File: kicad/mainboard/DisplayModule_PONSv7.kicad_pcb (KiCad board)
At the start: 4 copper layers, 55.4 x 77.6 mm, 135 parts, among them J1 Ext. Speaker, J2 54132-4062, J3 2005280040, J4 Micro_SD_Card_Det2, J5 Conn_01x03_Shielded, J6 USB_B_Micro, Q1 AO3401A, SW1 PTS645VK392LFS, SW2 SW_TS-1088, SW3 SW_TS-1088, U1 PAM8302AADCR, U10 BNO085, U12 E220-900T22S(JP), U2 W25Q128JVS, U3 RP2350_80QFN, U4 MCP73831-2-OT, U5 TPS63031DSK, U6 MAINSW_CUS-12TB, U7 TFTSW_CUS-12TB, U8 MS5611-01BA, Y1 X322512MSB4SI, Y2 32.768k

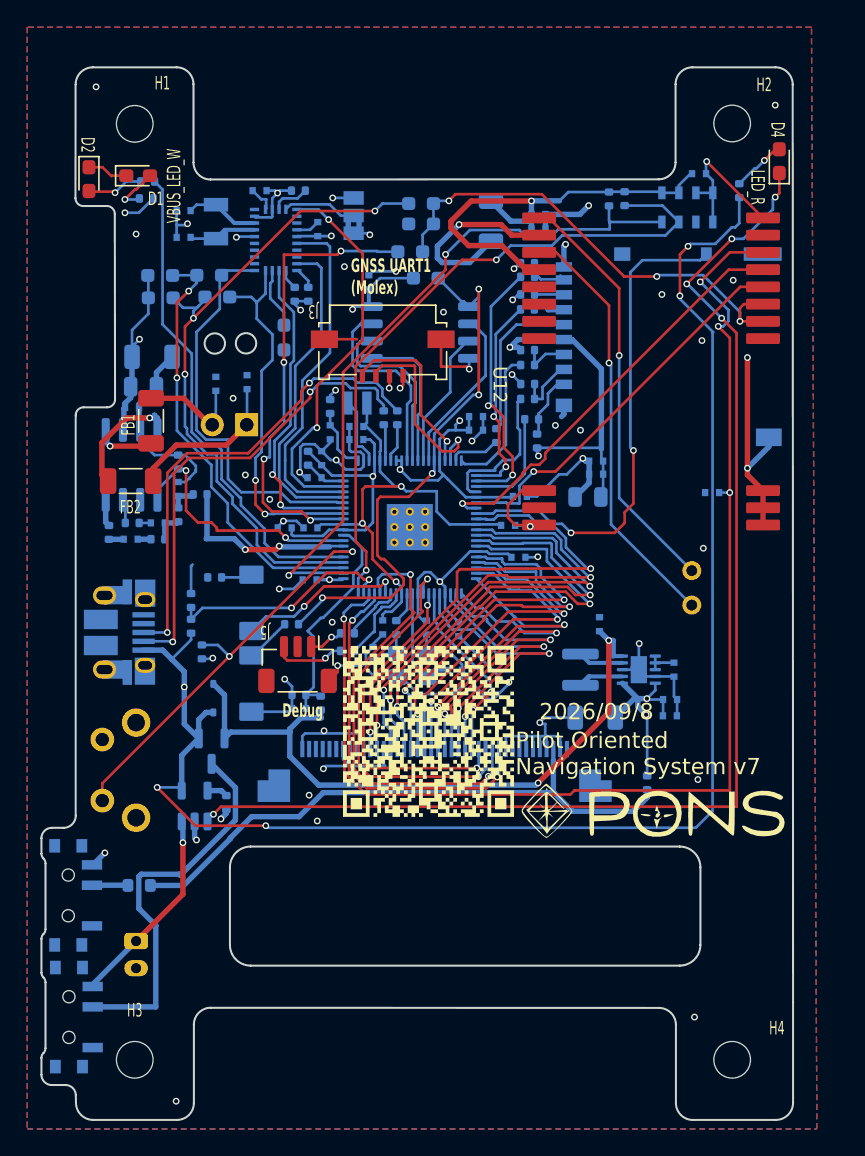
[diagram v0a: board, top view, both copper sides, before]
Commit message: 0.986 新基板（SCH16T 外付け）の kicad を追加し、ガーバー出力を git から外した
kicad/IMU_murata/ — SCH16T-K01-10 のブレイクアウト（新規）
本体の J7（Molex 200528-0080・8pin FPC）へ 1:1 ケーブルで繋ぐ外付け基板。
J1 のピン順を本体 J7 と一致させてある（1=+3V3 2=RESET 3=MOSI 4=CS 5=SCK
6=SYNC 7=MISO 8=GND）。シンボルとフットプリントも同梱。
- ★ R2（CS-GND の 4.7k）は実装しない。CS は負論理なので、プルダウンすると
  MCU が駆動していない間セレクト状態になる。R1（EXTRESN プルアップ）は実装する
- 本体側の GPIO 割り当ては settings.h の SCH16T_PIN_* が正本
  （一覧は docs/imu_sch16t_plan.md §3）

mainboard / GNSS モジュールの更新
- mainboard: DisplayModule_PONSv7 の pcb / pro / sch、MS5611BNO085.kicad_sch、
  SHT_RP2354B.kicad_sch
- GNSS モジュール: pcb / pro / sch、および QRv7 と FPC 4p のフットプリントを
  同プロジェクトの Footprints/ へ取り込み

kicad/FPC/ を畳んだ
FPC コネクタ 1 個のためのプロジェクトだったので、フットプリントを
kicad/GNSSboard_SAM-M10Q/Footprints/ へ移して削除した。
中身は同じで、差分は KiCad が再生成する uuid だけ。

ガーバー・ドリルのプロット出力を git から外した
kicad/.gitignore に追加（*.gbr *.gbl *.gbs *.gbp *.gbo *.gm1 *.gtl *.gts
*.gtp *.gto *.drl と、保険の *plot/ *plot.zip）。発注のたびに作り直せるうえ、
基板を直すたびに巨大な差分になる（ルート .gitignore の production/ と同じ理由）。
★ 入れ物のフォルダ名で書かないこと。v5_1plot/ のような名前は付け方が毎回違うので
  次の基板で外れる。既存の *-backups/ / *.kicad_prl と同じ方針。

Co-Authored-By: Claude Opus 5 <noreply@anthropic.com>
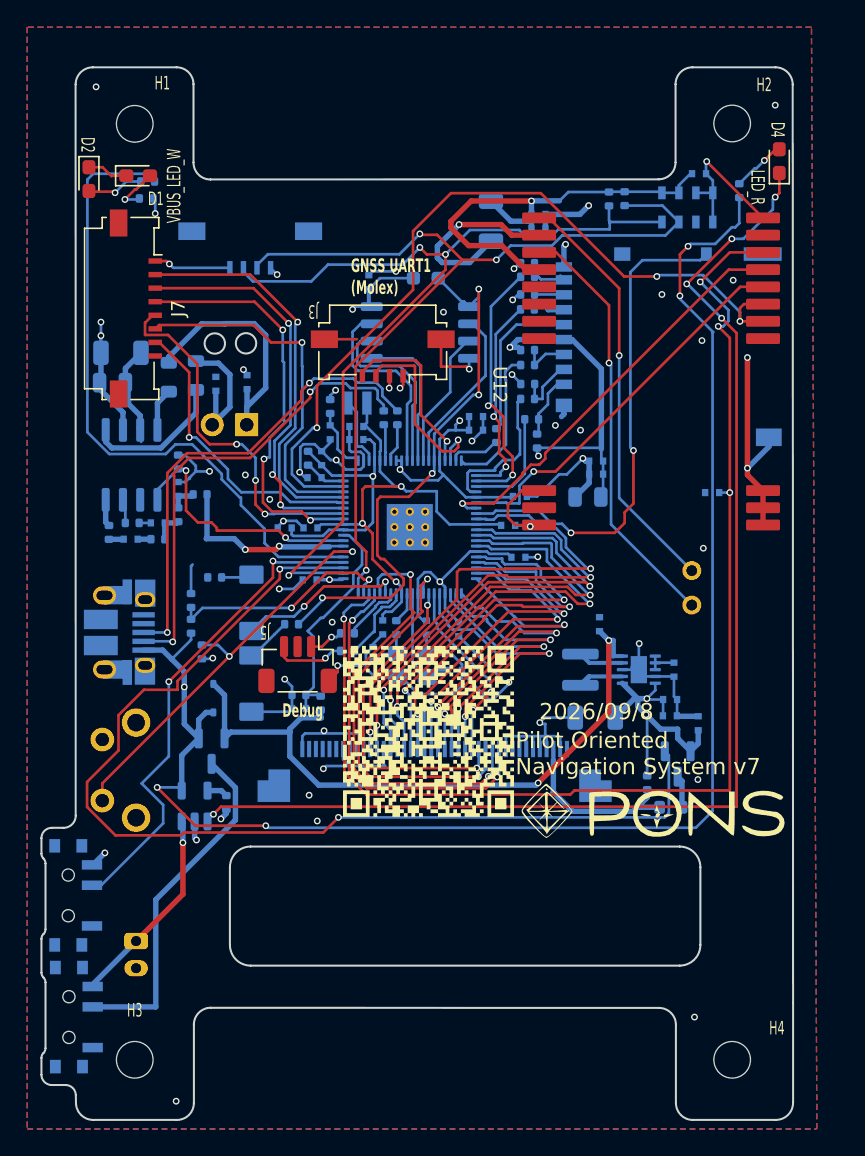
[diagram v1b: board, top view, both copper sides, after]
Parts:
- removed C40: 100n, GPS_TFT:C_0402_1005Metric_small_pads
- removed C41, C42: 15p, GPS_TFT:C_0402_1005Metric_small_pads
- removed JP1: BNO_I2C_SPI_SELECT, Jumper:SolderJumper-3_P1.3mm_Bridged2Bar12_Pad1.0x1.5mm
- removed R37, R38: 4.7k, Resistor_SMD:R_0603_1608Metric_Pad0.98x0.95mm_HandSolder
- removed R44: 10k, Resistor_SMD:R_0402_1005Metric
- removed R46, R47, R50, R51, R52, R53: 0, Resistor_SMD:R_0603_1608Metric_Pad0.98x0.95mm_HandSolder
- removed R48, R49: 4.7k, Resistor_SMD:R_0402_1005Metric
- removed U10: BNO085, GPS_TFT:bno085
- removed Y2: 32.768k, Crystal:Crystal_SMD_3215-2Pin_3.2x1.5mm
- added J7: Conn_01x08_MountingPin, Connector_FFC-FPC:Molex_200528-0080_1x08-1MP_P1.00mm_Horizontal, F.Cu at (102.6, 72.5)
- added J8: 2005280040, Connector_FFC-FPC:Molex_200528-0040_1x04-1MP_P1.00mm_Horizontal, B.Cu at (110.5, 68.6)
- added Q2: AO3401A, Package_TO_SOT_SMD:SOT-23, B.Cu at (142.0, 106.1)
- C39: value 100n -> 10u
- FB1, FB2: value 390 -> 600; footprint Inductor_SMD:L_1206_3216Metric_Pad1.22x1.90mm_HandSolder -> Inductor_SMD:L_0805_2012Metric; moved to B.Cu
- moved C39 50.8 mm to (143.5, 103.1), turned to 90 degrees
- moved R9 39.6 mm to (141.5, 109.3), turned to 180 degrees
- moved FB2 8.15 mm to (104.5, 77.6), turned to 90 degrees
- moved FB1 4.70 mm to (106.5, 77.4)
- moved C7 2.31 mm to (100.3, 78.0)
- moved C9 2.31 mm to (101.0, 75.8)
- moved C6 0.86 mm to (101.0, 79.5)
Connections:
- R9 pad 1: PWR_TFT -> Net-(Q2-D)
- U12 pad 5: Net-(U12-M0) -> LORA_M01
- U12 pad 6: Net-(U12-M0) -> LORA_M01
- U3 pad 43: I2C1_SDA -> TFT_MOSFET_G
- U3 pad 44: I2C1_SCL -> TFT_SW
- U3 pad 56: BNO_INT -> SCH16T_RESET
- U3 pad 57: BNO_NRST -> SCH16T_SYNC
- U3 pad 58: BNO_WAKE -> LORA_M01
- U7 pad P$2: PWR_TFT -> TFT_SW
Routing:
- net TFT_MOSFET_G: track 0.00 -> 78.7 mm, vias 0 -> 2
- net LORA_M01: track 0.00 -> 60.1 mm, vias 0 -> 3
- net I2C1_SCL: track 50.0 -> 0.00 mm, vias 3 -> 0
- net TFT_SW: track 0.00 -> 36.4 mm, vias 0 -> 2
- net Net-(U12-M0): track 35.6 -> 0.00 mm, vias 3 -> 0
- net I2C1_SDA: track 32.3 -> 0.00 mm, vias 2 -> 0
- net Net-(J2-Pad3): track 44.3 -> 13.3 mm
- net SCH16T_RESET: track 0.00 -> 29.4 mm, vias 0 -> 1
- net BNO_WAKE: track 28.9 -> 0.00 mm, vias 2 -> 0
- net SCH16T_SYNC: track 0.00 -> 26.8 mm, vias 0 -> 1
- net BNO_NRST: track 25.7 -> 0.00 mm
- net BNO_INT: track 24.1 -> 0.00 mm
- net I2C0_SDA: track 50.0 -> 67.1 mm, vias 2 -> 3
- net I2C0_SCL: track 51.3 -> 68.1 mm, vias 2 -> 3
- net USR_LED: track 36.8 -> 48.4 mm
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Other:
- outline, holes or cut-outs redrawn
- board text removed: "ここにGNSS/別基板(UART)"

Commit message: 0.993 v7.1 基板の回路図と PCB を仕上げ、SW OFF のままの充電と電源異常を画面と音声で知らせるようにした
- power.cpp（新規）: USB の判定を usb_power_present() に一本化（v7.1 は VBUS を
  GPIO47 の ADC で測る）。電源経路の異常（2026-10-15 の充電 IC 焼損）を検出し、
  地図の POWER FAULT!! と power_fault.wav（30 秒ごと・最低音量 60）で知らせる。
  受信機は LINK_ST_PWR_FAULT を受けてトーン（同じ音声だとボートへの指示に聞こえる）
- v7.1: SW を OFF にしたまま USB で充電していると満充電にならない（Q3 のボディ
  ダイオード経由）。SW4 の OFF 側が GPIO40 を GND に落とすのを読み、地図に注意を出し
  1 度だけ読み上げる（charge_sw_off / charge_sw_on。排他グループ WAV_EXCL_CHARGE_SW）。
  移動中・ミラー中・リプレイ中・デモ中は出さない。判定に USB を入れない
  （VBUS が一瞬 4.3V を割ると 0V が本物の電池電圧として流れるため）。このあいだは
  電池低下の警告を止め、無線は RHAVE_VOLT を立てず LINK_ST_USB_SW_OFF、CSV は空欄
- 受信モードの電池表示を s55r42 の形に。SW OFF のまま USB の側は s5V / r5V
- backlight.cpp（新規）: v7.1 のバックライト PWM と VEML7700 の自動調光。
  飛行 CSV に lux / backlight 列
- E220 の M0/M1 は v7.1 で GPIO31 へ（GPIO47 は USB_SENS）
- 本体の回路図・PCB: SCH16T の J6 を逆順に（完成済みの FPC で J6-n ↔ J3-(9-n)）、
  F1 0805L035 → 0805L050（夏の充電で切れない）、R34/R35 を 10k/5.1k、C32 を 10µF 0805、
  SPI1 の SCK/MOSI/CS に 33Ω（R49〜R51）、スライドスイッチを MST-12D18G2 に、
  回路図とつながらない旧フットプリント（C33/R37/R38/R11 470Ω）を削除、DNP の BOM 除外、
  CUS-12TB の残骸とライブラリ登録を削除、メモの部品番号を v7.1 に
- GNSS 基板を 5 ピン（V_BCKUP）に。バックアップ電池は本体へ移した
- case_cover（照度センサー VEML7700）の kicad を追加。IMU ブレイクアウトの R2 を DNP
- 音声 3 本（power_fault / charge_sw_off / charge_sw_on）は macOS の音声合成の仮音声
- docs/pons_power.md（新規）。README の「自作の手順」を v7.1 に書き直し、
  SCH16T の配線の記述（J7・1:1 ケーブル）を J6・逆順に直した
- gen_wav_flash.py はコメント中の引用符付きの音声名も拾うので、録音前の名前を書かない

PONS_BOARD は V7 と V71 の両方でビルド OK（3,929,776 / 3,923,504 B）/
gen_wav_flash.py --check は 35 ファイル一致 / 本体 PCB の DRC は未配線 0・回路図と一致
（シルクの 6 件はボタンと USB の突起で意図どおり）/ GNSS 基板も未配線 0 / 実機は未確認

Co-Authored-By: Claude Opus 5.5 <noreply@anthropic.com>
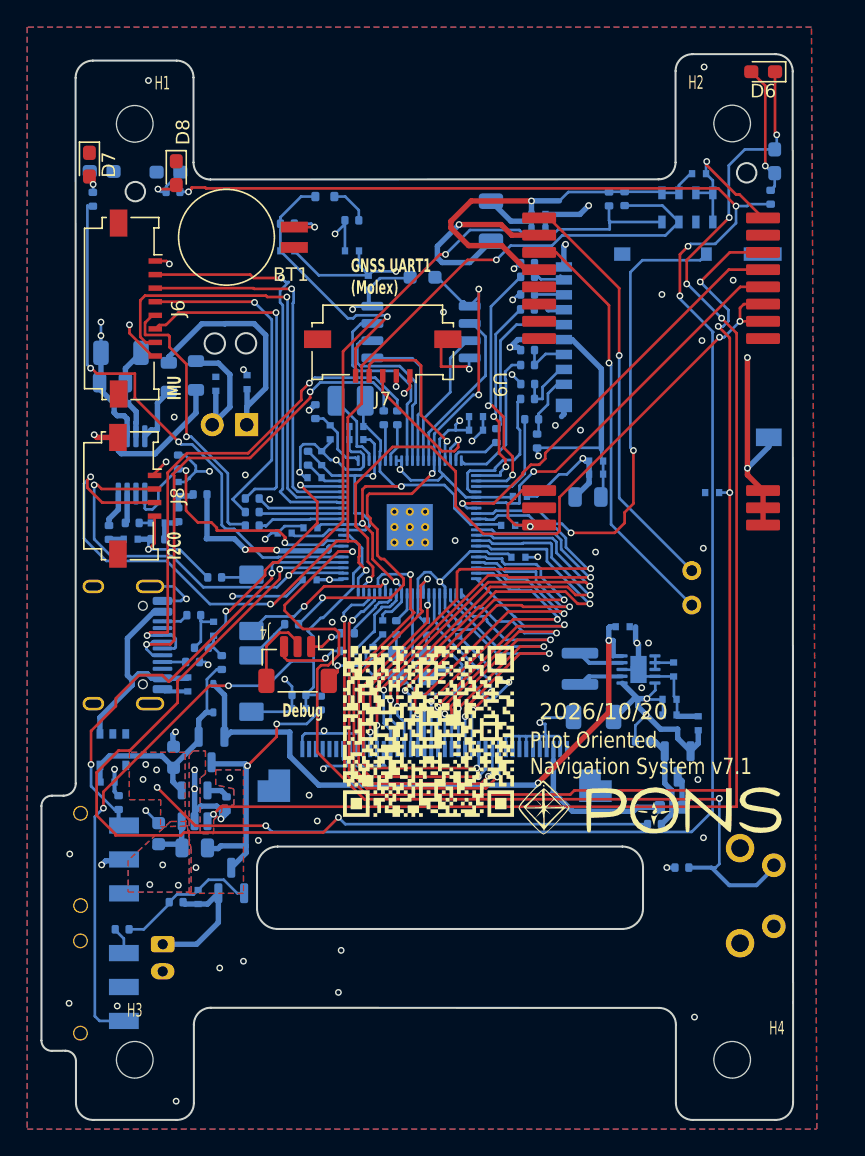
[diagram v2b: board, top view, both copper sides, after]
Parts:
- removed the C11 at (119.2, 70.6)
- removed the C31 at (136.2, 95.8)
- removed the C36 at (141.4, 101.3)
- removed the C4 at (135.9, 102.6)
- removed the J3 at (120.3, 76.6)
- removed the J6 at (100.9, 96.3)
- removed the Q1 at (107.7, 105.1)
- removed the R10 at (139.8, 107.5)
- removed the R18 at (102.9, 63.1)
- removed the R42 at (146.5, 63.8)
- removed the R7 at (123.4, 70.3)
- removed U6: MAINSW_CUS-12TB, GPS_TFT:CUS-12TB
- removed U7: TFTSW_CUS-12TB, GPS_TFT:CUS-12TB
- added BT1: MS621FE, Battery:BatteryHolder_Seiko_MS621F, F.Cu at (113.8, 67.2)
- added C12: 100n, GPS_TFT:C_0402_1005Metric_small_pads, B.Cu at (119.2, 70.6)
- added C32: 4.7u, GPS_TFT:C_0402_1005Metric_small_pads, B.Cu at (137.9, 96.0)
- added C35: 100n, GPS_TFT:C_0402_1005Metric_small_pads, B.Cu at (141.7, 99.1)
- added C39: 10u, GPS_TFT:C_0402_1005Metric_small_pads, B.Cu at (141.4, 101.3)
- added C40: 4.7u 16V, Capacitor_SMD:C_0603_1608Metric, B.Cu at (103.8, 111.2)
- added C41: 10u, GPS_TFT:C_0402_1005Metric_small_pads, B.Cu at (141.4, 102.5)
- added C47: 100n, GPS_TFT:C_0402_1005Metric_small_pads, B.Cu at (113.2, 68.2)
- added C48: 100n, GPS_TFT:C_0402_1005Metric_small_pads, B.Cu at (118.0, 68.2)
- added C49: 1u, GPS_TFT:C_0402_1005Metric_small_pads, B.Cu at (107.8, 96.1)
- added C5: 100u, Capacitor_SMD:C_1206_3216Metric, B.Cu at (135.8, 102.6)
- added C50: 1u, GPS_TFT:C_0402_1005Metric_small_pads, B.Cu at (100.0, 107.4)
- added C51: 1u, GPS_TFT:C_0402_1005Metric_small_pads, B.Cu at (105.9, 100.2)
- added D5: RB520S-30, Diode_SMD:D_SOD-523, B.Cu at (116.0, 64.2)
- added D6: LED_R, LED_SMD:LED_0603_1608Metric_Pad1.05x0.95mm_HandSolder, F.Cu at (148.3, 55.0)
- added D7: LED_R, LED_SMD:LED_0603_1608Metric_Pad1.05x0.95mm_HandSolder, F.Cu at (98.7, 61.9)
- added D8: VBUS_LED_W, LED_SMD:LED_0603_1608Metric_Pad1.05x0.95mm_HandSolder, F.Cu at (105.0, 62.5)
- added F1: 0805L050, Fuse:Fuse_0805_2012Metric, B.Cu at (106.4, 112.2)
- added J7: 2005280050, Connector_FFC-FPC:Molex_200528-0050_1x05-1MP_P1.00mm_Horizontal, F.Cu at (120.3, 76.6)
- added J9: USB_C_Receptacle_USB2.0_16P, Connector_USB:USB_C_Receptacle_HRO_TYPE-C-31-M-12, B.Cu at (100.0, 97.3)
- added Q2: AO3401A, Package_TO_SOT_SMD:SOT-23, B.Cu at (107.7, 105.0)
- added Q3: AO3401A, Package_TO_SOT_SMD:SOT-23, B.Cu at (109.1, 114.7)
- added R3: 470, Resistor_SMD:R_0402_1005Metric, B.Cu at (104.8, 63.9)
- added R34: 10k, Resistor_SMD:R_0402_1005Metric, B.Cu at (108.4, 98.6)
- added R37: 10k, Resistor_SMD:R_0402_1005Metric, B.Cu at (101.1, 118.2)
- added R38: 100k, Resistor_SMD:R_0402_1005Metric, B.Cu at (105.0, 116.2)
- added R40: 200, Resistor_SMD:R_0402_1005Metric, B.Cu at (148.8, 64.3)
- added R43: 220, Resistor_SMD:R_0402_1005Metric, B.Cu at (118.0, 66.0)
- added R44: 470, Resistor_SMD:R_0402_1005Metric, B.Cu at (113.2, 66.2)
- added R45: 5.1k, Resistor_SMD:R_0402_1005Metric, B.Cu at (106.2, 98.5)
- added R46: 5.1k, Resistor_SMD:R_0402_1005Metric, B.Cu at (106.3, 95.1)
- added R47: 100k, Resistor_SMD:R_0402_1005Metric, B.Cu at (139.4, 104.4)
- added R48: 4.7k, Resistor_SMD:R_0402_1005Metric, B.Cu at (100.8, 108.9)
- added R49: 33, Resistor_SMD:R_0402_1005Metric, B.Cu at (110.7, 87.5)
- added R50: 33, Resistor_SMD:R_0402_1005Metric, B.Cu at (110.7, 88.5)
- added R51: 33, Resistor_SMD:R_0402_1005Metric, B.Cu at (110.7, 86.5)
- added R9: 10k, Resistor_SMD:R_0603_1608Metric_Pad0.98x0.95mm_HandSolder, B.Cu at (123.2, 70.2)
- added SW4: MST-12D18G2 SMD SLIDE SWITCH, GPS_TFT:SW-SMD_3P-L9.1-W3.5-P2.50_MST-12D18G2, B.Cu at (101.2, 122.5)
- added SW5: MST-12D18G2 SMD SLIDE SWITCH, GPS_TFT:SW-SMD_3P-L9.1-W3.5-P2.50_MST-12D18G2, B.Cu at (101.2, 113.1)
- added U10: NCP361SNT1G, Package_SO:TSOP-5_1.65x3.05mm_P0.95mm, B.Cu at (100.4, 105.0)
- C37: value 10u -> 4.7u 16V; footprint GPS_TFT:C_0402_1005Metric_small_pads -> Capacitor_SMD:C_0603_1608Metric
- D1, D2, D4: moved to B.Cu
- J8: moved to F.Cu
- L1: footprint GPS_TFT:L_pol_2016 -> Inductor_SMD:L_1008_2520Metric
- R11: value 470 -> 100
- R32: renamed from R33; value 100K -> 100k
- R35: value 5K1 -> 5.1k
- R36: value 10K -> 1k
- R39: value 2.2k -> 3.3k
- R7: renamed from R6; value 100K -> 100k
- R8: value 1k -> 200
- U1: value PAM8302AADCR -> PAM8302AASCR; footprint Package_SO:SO-8_3.9x4.9mm_P1.27mm -> Package_SO:MSOP-8_3x3mm_P0.65mm
- U4: value MCP73831-2-OT -> TPS63031DSK; footprint Package_TO_SOT_SMD:SOT-23-5 -> Package_SON:WSON-10-1EP_2.5x2.5mm_P0.5mm_EP1.2x2mm
- U5: value TPS63031DSK -> MCP73831-2-OT; footprint Package_SON:WSON-10-1EP_2.5x2.5mm_P0.5mm_EP1.2x2mm -> Package_TO_SOT_SMD:SOT-23-5
- moved R11 59.4 mm to (140.3, 110.5)
- moved SW3 51.4 mm to (149.1, 118.0), turned to 90 degrees
- moved R36 41.2 mm to (142.3, 113.7), turned to 0 degrees
- moved C33 38.9 mm to (106.7, 115.9), turned to 90 degrees
- moved C37 36.7 mm to (104.8, 105.6), turned to 90 degrees
- moved R8 34.3 mm to (98.9, 64.5)
- moved U5 34.2 mm to (106.4, 109.2), turned to 90 degrees
- moved U4 34.2 mm to (139.1, 99.1), turned to 0 degrees
- moved J8 19.4 mm to (102.5, 86.3), turned to -90 degrees
- moved D1 2.25 mm to (104.5, 62.5)
- moved PWR1 1.97 mm to (104.0, 119.3)
- moved R35 1.76 mm to (106.9, 97.5), turned to 180 degrees
- moved R25 1.16 mm to (115.3, 80.1)
- moved D2 1.09 mm to (99.5, 62.4), turned to 180 degrees
- moved L1 0.53 mm to (117.9, 79.3)
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- renumbered C39 to C11, C12 to C13, C13 to C14, C14 to C15, C15 to C16, C16 to C17, C17 to C18, C18 to C19, C19 to C20, C20 to C21, C21 to C22, C22 to C23, C23 to C24, C24 to C25, C25 to C26, C26 to C27, C27 to C28, C28 to C29, C29 to C30, C30 to C31, C32 to C34, C34 to C36, C35 to C38, C5 to C4, C46 to C42, C38 to C43, C43 to C44, C44 to C46, J4 to J3, J5 to J4, J7 to J6, Q2 to Q1, R9 to R10, R19 to R18, R20 to R19, R21 to R20, R22 to R21, R23 to R22, R24 to R23, R25 to R24, R26 to R25, R27 to R26, R28 to R27, R29 to R28, R30 to R29, R31 to R30, R32 to R31, R34 to R33, R3 to R4, R40 to R41, R41 to R42, R4 to R5, R5 to R6, SW2 to SW1, SW3 to SW2, SW1 to SW3, TP3 to TP1, U12 to U9
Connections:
- net Net-(U3-GPIO40_ADC0) renamed ADC0
- C33 pad 1: Net-(U5-EN) -> VBAT_IN
- C33 pad 2: GND -> Net-(Q3-G)
- C37 pad 1: +3V3 -> VBUS_5V
- D3 pad 2: VBUS -> VBUS_5V
- J6 pad 1: +3V3 -> GND
- J6 pad 2: SCH16T_RESET -> SPI1_RX_MISO
- J6 pad 3: SPI1_TX_MOSI -> SCH16T_SYNC
- J6 pad 4: SPI1_CS -> Net-(J6-Pin_4)
- J6 pad 5: SPI1_SCK -> Net-(J6-Pin_5)
- J6 pad 6: SCH16T_SYNC -> Net-(J6-Pin_6)
- J6 pad 7: SPI1_RX_MISO -> SCH16T_RESET
- J6 pad 8: GND -> +3V3
- L2 pad 1: Net-(U5-L1) -> Net-(U4-L1)
- L2 pad 2: Net-(U5-L2) -> Net-(U4-L2)
- Q1 pad 1: TFT_MOSFET_G -> Net-(Q1-G)
- R11 pad 1: VBUS -> Net-(Q1-G)
- R11 pad 2: Net-(D1-A) -> TFT_MOSFET_G
- R30 pad 1: /RP2350B/USB_D+ -> USB_D+
- R31 pad 1: /RP2350B/USB_D- -> USB_D-
- R32 pad 1: VSYS -> BATPWR
- R35 pad 1: VBUS -> USB_SENS
- R35 pad 2: USB_SENS -> GND
- R36 pad 1: USB_SENS -> +3V3
- R36 pad 2: GND -> SW_TOGGLE
- R39 pad 1: Net-(U4-PROG) -> Net-(U5-PROG)
- R8 pad 1: +3V3 -> USR_LED
- R8 pad 2: SW_TOGGLE -> Net-(D2-A)
- U3 pad 39: USB_SENS -> LORA_M01
- U3 pad 58: LORA_M01 -> USB_SENS
- U4 pad 1: Net-(D4-K) -> +3V3
- U4 pad 2: GND -> Net-(U4-L2)
- U4 pad 3: VBAT_IN -> GND
- U4 pad 4: VBUS -> Net-(U4-L1)
- U4 pad 5: Net-(U4-PROG) -> VSYS
- U5 pad 1: +3V3 -> Net-(D4-K)
- U5 pad 2: Net-(U5-L2) -> GND
- U5 pad 3: GND -> /VBAT_THERMAL
- U5 pad 4: Net-(U5-L1) -> VBUS_5V
- U5 pad 5: VSYS -> Net-(U5-PROG)
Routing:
- net VBUS: track 162.2 -> 0.00 mm, vias 6 -> 0
- net VBUS_5V: track 0.00 -> 155.3 mm, vias 0 -> 9
- net GND: track 190.5 -> 285.2 mm, vias 45 -> 70
- net USB_D+: track 0.00 -> 39.0 mm, vias 0 -> 2
- net ADC0: track 16.9 -> 55.4 mm, vias 0 -> 2
- net USB_D-: track 0.00 -> 37.8 mm, vias 0 -> 2
- net SW_TOGGLE: track 29.8 -> 66.4 mm
- net /RP2350B/USB_D+: track 35.0 -> 0.00 mm, vias 2 -> 0
- net /RP2350B/USB_D-: track 34.8 -> 0.00 mm, vias 2 -> 0
- net BATPWR_LDO: track 25.7 -> 0.00 mm
- net Net-(J6-Pin_6): track 0.00 -> 24.9 mm, vias 0 -> 1
- net Net-(J6-Pin_4): track 0.00 -> 24.9 mm, vias 0 -> 1
- net SPI1_CS: track 30.4 -> 6.45 mm, vias 3 -> 0
- net SPI1_TX_MOSI: track 29.9 -> 6.50 mm, vias 3 -> 0
- net BATPWR: track 0.00 -> 21.3 mm, vias 0 -> 2
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- added copper zone on B.Cu, net /VBAT_THERMAL
- added copper zone on F.Cu, net /VBAT_THERMAL
- added copper zone on B.Cu, net VBUS_5V
- added copper zone on F.Cu, net VBUS_5V
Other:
- board size 55.4 x 77.6 mm -> 55.4 x 78.5 mm
- board text added: "2026/10/20"
- board text added: "=Required External Parts= GNSS module UART (molex5P Conn) Speaker GC0351M-ND 860mAh 1s LiPo with (PH2P) M2.5 Screw x4 =Optional External Parts= Cover module (molex4P Conn) IMU (molex 8P Conn)"
- board text added: "I2C0"
- board text added: "IMU"
- board text added: "PONS for HPA v7.1"
- board text added: "Pilot Oriented Navigation System v7.1"
- board text added: "[Memo JLCPCB BOM Exemption] J1 Speaker socket (No parts required) J4 Debug SH 3p(No use. Debug purpose) U9 E220 LoRa (Due to 技適, 手実装) H1,H2,H3,H4 Hole"
- board text removed: "2026/09/8"
- board text removed: "=Required External Parts= GNSS module UART (SH4P or molex4P) Speaker GC0351M-ND 860mAh 1s LiPo with (PH2P) M2.5 Screw x4"
- board text removed: "GND"
- board text removed: "PONS for HPA v7"
- board text removed: "Pilot Oriented Navigation System v7"
- board text removed: "VBAT_IN"
- board text removed: "[Memo JLCPCB BOM Exemption] J1 Speaker socket (No parts required) J5 Debug SH 3p(No use. Debug purpose) U12 E220 LoRa (Due to 技適, 手実装) U6,U7 CUS-12TB Switch (JLCPCBにないパーツのため手実装） H1,H2,H3,H4 Hole TP3 LoRa JP SW1 (JLCにないパーツのため） PWR1（コスト） Not an assemble parts JP1 I2C-SPI jumper BNO085 R47,R7,R46,R38,R37,R50,R51 DNF"

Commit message: 0.994 GNSS の翌日起動を速くし、本番前チェック・高温充電の警告・電池低下の点滅を入れ、v7.1 基板の逆接保護と発注前の修正を仕上げた
- GNSS: AssistNow Autonomous を有効化（CFG-VALSET で RAM と BBR。settings.h の
  GNSS_USE_ANA。0 でも OFF を書き込む＝BBR に残った ON を消すため）。前日と同じ時間帯の
  起動が 23〜28 秒 → 3〜4 秒（BT1 が生きていること）。NAV-AOPSTATUS を 1Hz で受け、
  GNSS DETAIL 3 に ANA:ON data/use/calc、log.txt に「... after boot」（TTFF）・最初の
  測位の軌道の出どころ・10 分ごとの計算時間。ACK 待ちの間も imu_service_if_due() を
  呼ぶ（以前からの抜け）
- readiness.cpp（新規）: 本番前チェック。GNSS・IMU・ESKF・較正（マウント外れだけ。
  日付またぎは推測なので入れない＝台の上での APPLY を促さない）・地上の姿勢・設定画面の
  赤丸・USB・電池 50%・SD・無線（送信モード）がそろい、地上で止まっていたら 1 度だけ
  「準備完了」（ready.wav）。欠けていれば設定画面の右上に項目名。受信モード・リプレイ・
  デモは対象外。既存の判定を読むだけで、条件は書き写さない
- 高温での充電の警告（v7・v7.1）: USB 接続中に MS5611 が 45°C を 30 秒超え続けたら
  地図に TOO HOT TO CHARGE と charge_hot.wav（60 秒ごと・最低音量 60）。電池の仕様は
  充電 0〜45°C。地図の段は電源異常と共用（異常 ＞ 高温 ＞ SW OFF）
- 電池低下のときの点滅（v7.1）: 電池低下の警告と同じ 3.5V でバックライトを 2 秒点灯・
  4 秒消灯。3.65V か USB で戻る（3.5V で戻すと入り切りをくり返す）。消灯中も本来の
  明るさは追い続ける（照度追従の立ち上がりで 2 秒の点灯が暗くならないように）
- 本体の回路図・PCB: 電池の逆接保護 Q4（AO3401A、D が電池側）＋ R52、PWR1 の
  ネットを VBAT_RAW に。C32 を 10µF 0805 に（10/20 に直したのが 0402 に戻っていた）。
  D5 を RB751S40（逆流が少ない。PCBA で実装）に。古いメモを整理
- IMU 基板の GND が IC1.16・C3 だけ分かれていたのをつないだ。J3 の値を 01x08 に。
  case_cover の部品番号を回路図と一致。GNSS 基板の裏面を GND ベタに（浮いていた
  19 個のビアがつながった）
- 音声 2 本（ready / charge_hot）は macOS の音声合成の仮音声
- docs: pons_power.md に Q4・P-ch FET 3 段の役割・電池の保護回路（DTP603048(PHR) の
  仕様書）・R39 を 2.2kΩ に戻さない理由（電池の最大充電 430mA も超える）・高温の警告・
  電池低下の点滅。README に GNSS の起動・本番前チェック・新しい警報・v7.1 の USB-C と
  充電時間、古い記述（v7 の実結線試験・無線の立ち上げ手順書の冒頭）を今の状態に。
  CLAUDE.md に BBR に書いた GNSS 設定が残る件と readiness.cpp
- kicad/.gitignore に *.pos

PONS_BOARD は V7 と V71 の両方でビルド OK（4,052,376 / 4,046,728 B）/
gen_wav_flash.py --check は 37 ファイル一致 / 本体 PCB の DRC は未配線 0・回路図と一致
（シルクの 6 件は意図どおり）/ IMU・カバー・GNSS 基板も未配線 0・回路図と一致 /
BOM の LCSC 番号は全 48 種類を JLC/LCSC の部品情報と照合 / 実機は未確認

Co-Authored-By: Claude Opus 5.5 <noreply@anthropic.com>
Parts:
- added Q4: AO3401A, Package_TO_SOT_SMD:SOT-23, B.Cu at (115.3, 121.4)
- added R52: 100k, Resistor_SMD:R_0402_1005Metric, B.Cu at (113.4, 123.2)
- C32: value 4.7u -> 10u; footprint GPS_TFT:C_0402_1005Metric_small_pads -> Capacitor_SMD:C_0805_2012Metric
- D5: value RB520S-30 -> RB751S40
- moved R42 30.1 mm to (140.1, 94.4), turned to 0 degrees
- moved R41 30.0 mm to (138.2, 94.4), turned to 180 degrees
- moved C43 25.6 mm to (140.8, 88.0)
- moved U8 25.5 mm to (140.8, 90.5)
- moved TP1 4.49 mm to (147.5, 92.3)
- moved SW2 0.81 mm to (111.4, 94.2)
- moved SW1 0.81 mm to (111.4, 100.1)
- moved R34 0.80 mm to (109.2, 98.6)
- moved PWR1 0.74 mm to (104.8, 119.6)
- moved R24 0.70 mm to (114.2, 95.5)
- moved C30 0.52 mm to (115.2, 92.9)
- moved SW4 0.51 mm to (101.7, 122.5)
- moved SW5 0.51 mm to (101.7, 113.1)
- moved R37 0.49 mm to (101.4, 117.9), turned to -90 degrees
- moved SW3 0.40 mm to (148.7, 118.0)
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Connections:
- PWR1 pad 1: VBAT_IN -> VBAT_RAW
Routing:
- net I2C0_SCL: track 76.3 -> 91.9 mm
- net I2C0_SDA: track 85.1 -> 97.6 mm
- net VBAT_RAW: track 0.00 -> 11.7 mm
- net +3V3: track 173.2 -> 163.9 mm, vias 24 -> 26
- net Net-(Q4-G): track 0.00 -> 5.69 mm, vias 0 -> 2
- net VBUS_5V: track 155.3 -> 160.1 mm
- net UART1_RX: track 30.8 -> 35.5 mm
- net VBAT_IN: track 9.91 -> 14.4 mm
- net UART1_TX: track 28.6 -> 32.6 mm
- net V_BCKUP: track 21.1 -> 17.3 mm
- net LORA_M01: track 54.9 -> 58.1 mm
- net Net-(U9-SWDIO): track 31.1 -> 33.6 mm
- net Net-(U9-SWCLK): track 31.4 -> 33.8 mm
- net GND: track 285.2 -> 283.0 mm, vias 70 -> 72
- net QSPI_SS: track 42.9 -> 41.0 mm, vias 4 -> 2
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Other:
- board size 55.4 x 78.5 mm -> 54.7 x 78.5 mm
- board text added: "2026/10/22"
- board text added: "[Memo JLCPCB BOM Exemption] J1 Speaker socket (No parts required) J4 Debug SH 3p(No use. Debug purpose) U9 E220 LoRa (Due to 技適, 手実装) H1,H2,H3,H4 Hole U9,H1,H2,J4,H3,H4,J6,J7,BT1,J8 are all exemptions"
- board text removed: "2026/10/20"
- board text removed: "Speaker."
- board text removed: "[Memo JLCPCB BOM Exemption] J1 Speaker socket (No parts required) J4 Debug SH 3p(No use. Debug purpose) U9 E220 LoRa (Due to 技適, 手実装) H1,H2,H3,H4 Hole"

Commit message: 0.995 無線で化けたフレームを数え直していたのを直し、仮の音声 5 つを録音に差し替え、画面のセンサー名を基板に合わせ、起動ロゴを生成ツールで焼くようにし、README を v7.1 の発注方法に書き直した
Co-Authored-By: Claude Opus 5.5 <noreply@anthropic.com>
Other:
- board text added: "H5,phi4.5"
- board text added: "USB-C"
- board text removed: "USB Micro-B"
